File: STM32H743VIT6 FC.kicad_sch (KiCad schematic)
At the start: 82 parts, among them SW2 SW_Push, U1 TPS54302DDCR, U2 USBLC6-2SC6, U3 TPS54302DDCR

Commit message: W25N01GVZEIT
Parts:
- 3V3_C2: renamed from 3V3_C4; value 4u7 -> 1u
- U_FLASH1: value W25N01GVZEIG_TR -> W25N01GVZEIT
- renumbered 3v3_C3 to 3v3_C1
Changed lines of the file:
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@@
 		(on_board yes)
 		(dnp no)
-		(property "Reference" "3v3_C3"
+		(property "Reference" "3v3_C1"
 			(at 546.862 90.932 0)
 			(effects
@@
 			(project "STM32H743VIT6 FC"
 				(path "/c74cb3f0-4ada-468c-ba5c-2dfd9a4e418b"
-					(reference "3v3_C3")
+					(reference "3v3_C1")
 					(unit 1)
 				)
@@
 		(on_board yes)
 		(dnp no)
-		(property "Reference" "3V3_C4"
+		(property "Reference" "3V3_C2"
 			(at 586.74 90.17 0)
 			(effects
@@
 			)
 		)
-		(property "Value" "4u7"
+		(property "Value" "1u"
 			(at 586.74 92.71 0)
 			(effects
@@
 			(project "STM32H743VIT6 FC"
 				(path "/c74cb3f0-4ada-468c-ba5c-2dfd9a4e418b"
-					(reference "3V3_C4")
+					(reference "3V3_C2")
 					(unit 1)
 				)
@@
 			)
 		)
-		(property "Value" "W25N01GVZEIG_TR"
+		(property "Value" "W25N01GVZEIT"
 			(at 211.836 223.012 0)
 			(effects

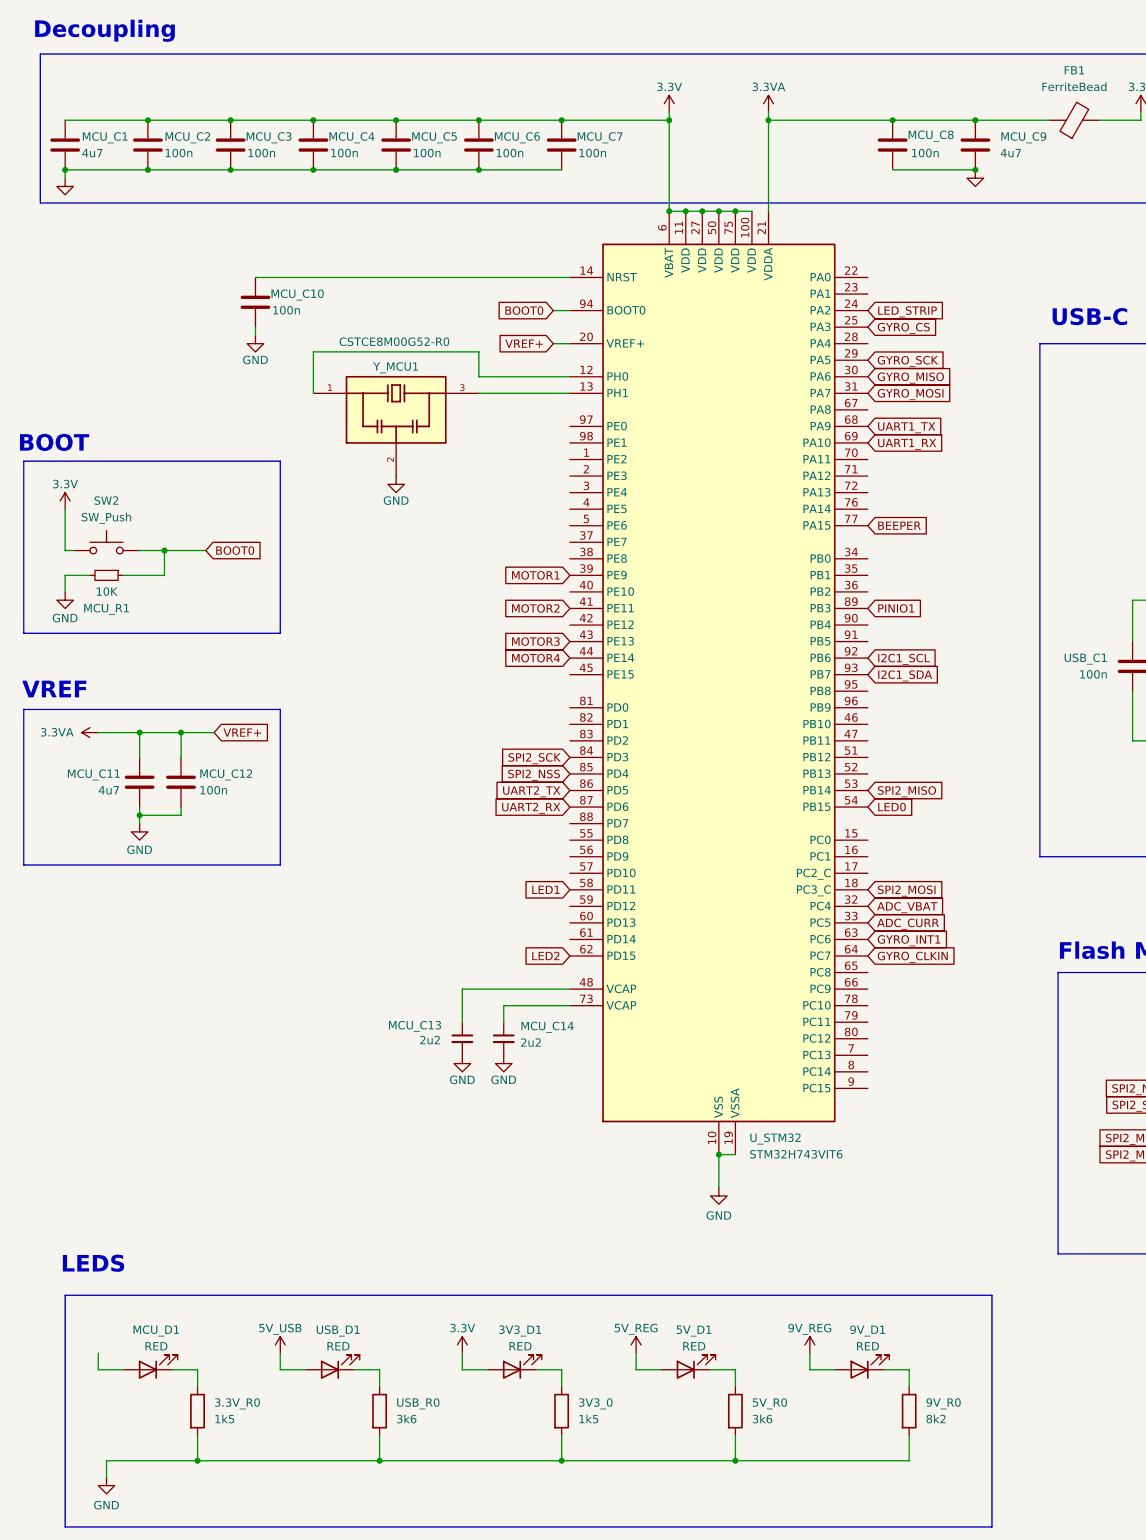
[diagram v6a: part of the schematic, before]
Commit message: Connected USB and fixed MCU decoupling.
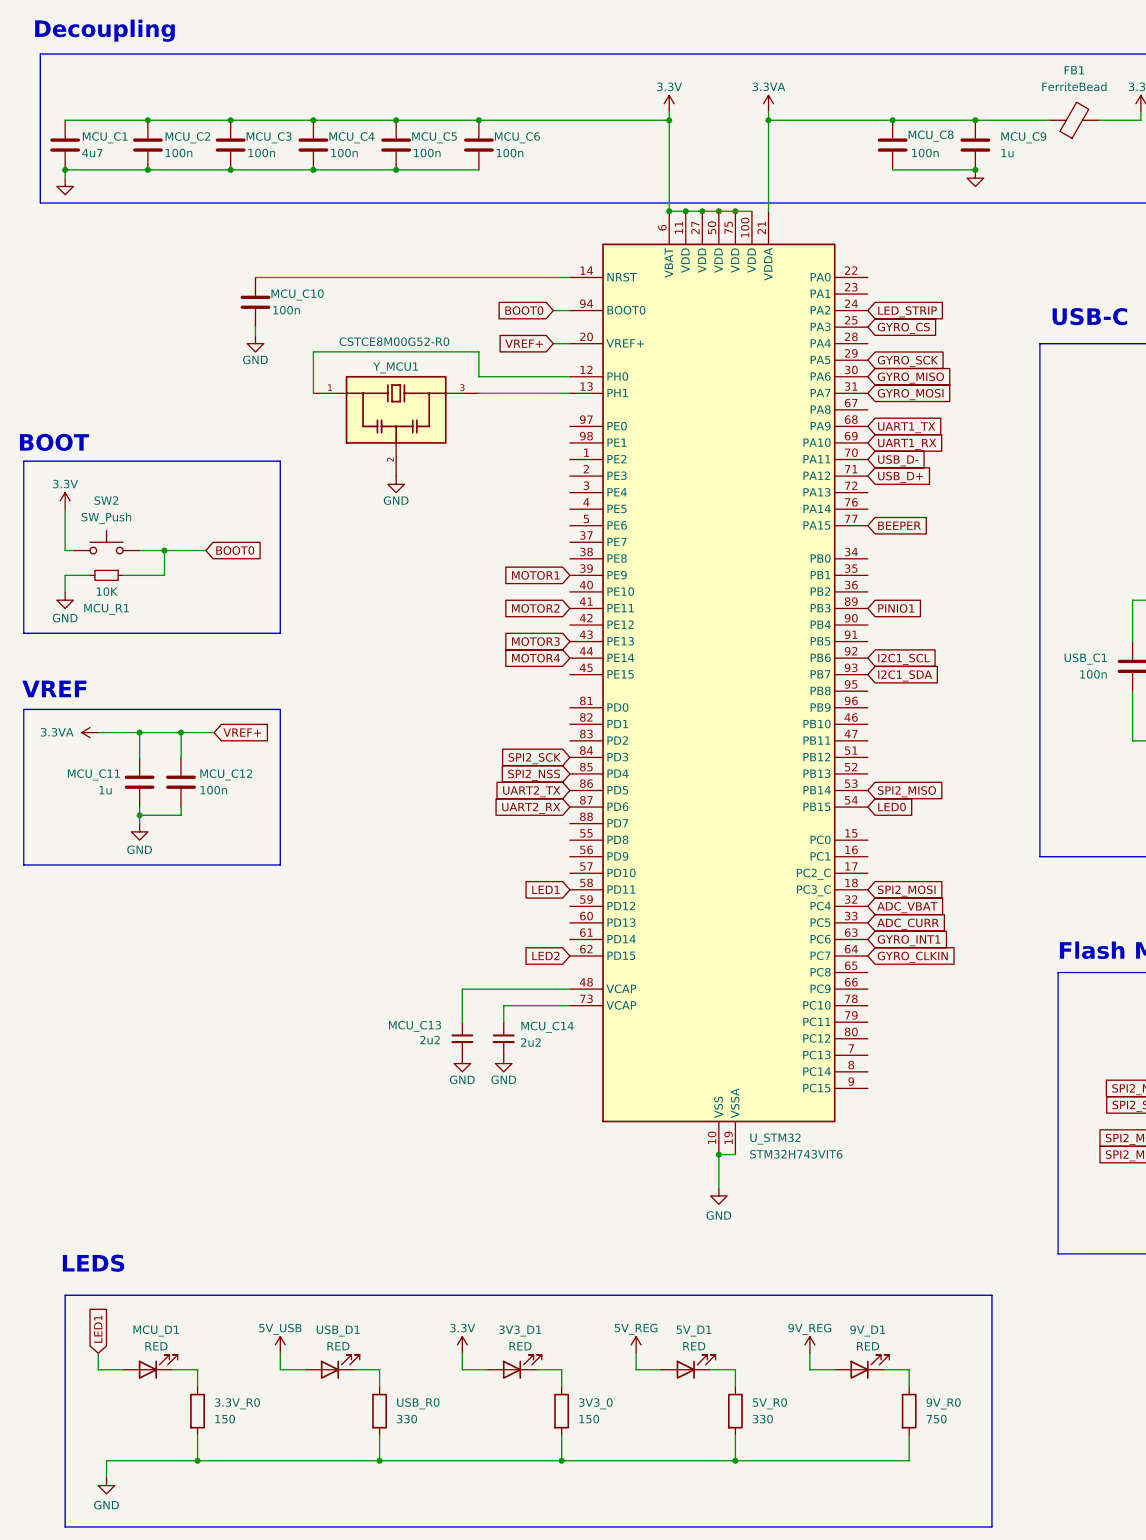
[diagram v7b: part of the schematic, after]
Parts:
- removed MCU_C7: 100n, Capacitor_SMD:C_0402_1005Metric, symbol Device:C
- 3.3V_R0, 3V3_0: value 1k5 -> 150
- 5V_R0, USB_R0: value 3k6 -> 330
- 9V_R0: value 8k2 -> 750
- MCU_C11, MCU_C9: value 4u7 -> 1u
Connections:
- net LED1: now also MCU_D1.2 (A)
- net USB_D+: now also U_STM32.71 (PA12)
- net USB_D-: now also U_STM32.70 (PA11)
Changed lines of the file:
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@@
 	)
 	(junction
-		(at 101.6 54.61)
-		(diameter 0)
-		(color 0 0 0 0)
-	)
-	(junction
 		(at 36.83 161.29)
 		(diameter 0)
@@
 	)
 	(junction
-		(at 88.9 62.23)
-		(diameter 0)
-		(color 0 0 0 0)
-	)
-	(junction
 		(at 363.22 213.614)
 		(diameter 0)
@@
 	(wire
 		(pts
-			(xy 101.6 54.61) (xy 118.11 54.61)
+			(xy 88.9 54.61) (xy 118.11 54.61)
 		)
 		(stroke
@@
 	(wire
 		(pts
-			(xy 88.9 54.61) (xy 101.6 54.61)
-		)
-		(stroke
-			(width 0)
-			(type default)
-		)
-	)
-	(wire
-		(pts
 			(xy 69.85 246.38) (xy 73.66 246.38)
 		)
@@
 	(wire
 		(pts
-			(xy 88.9 62.23) (xy 101.6 62.23)
-		)
-		(stroke
-			(width 0)
-			(type default)
-		)
-	)
-	(wire
-		(pts
 			(xy 728.98 71.12) (xy 740.41 71.12)
 		)
@@
 		)
 	)
+	(global_label "USB_D-"
+		(shape input)
+		(at 148.59 106.68 0)
+		(fields_autoplaced yes)
+		(effects
+			(font
+				(size 1.27 1.27)
+			)
+			(justify left)
+		)
+		(property "Intersheetrefs" "${INTERSHEET_REFS}"
+			(at 159.1952 106.68 0)
+			(effects
+				(font
+					(size 1.27 1.27)
+				)
+				(justify left)
+				(hide yes)
+			)
+		)
+	)
 	(global_label "GYRO_MOSI"
 		(shape input)
@@
 		)
 	)
+	(global_label "LED1"
+		(shape input)
+		(at 30.48 243.84 90)
+		(fields_autoplaced yes)
+		(effects
+			(font
+				(size 1.27 1.27)
+			)
+			(justify left)
+		)
+		(property "Intersheetrefs" "${INTERSHEET_REFS}"
+			(at 30.48 236.1982 90)
+			(effects
+				(font
+					(size 1.27 1.27)
+				)
+				(justify left)
+				(hide yes)
+			)
+		)
+	)
 	(global_label "GYRO_MOSI"
 		(shape input)
@@
 		)
 	)
+	(global_label "USB_D+"
+		(shape input)
+		(at 148.59 109.22 0)
+		(fields_autoplaced yes)
+		(effects
+			(font
+				(size 1.27 1.27)
+			)
+			(justify left)
+		)
+		(property "Intersheetrefs" "${INTERSHEET_REFS}"
+			(at 159.1952 109.22 0)
+			(effects
+				(font
+					(size 1.27 1.27)
+				)
+				(justify left)
+				(hide yes)
+			)
+		)
+	)
 	(global_label "SPI2_MOSI"
 		(shape input)
@@
 			)
 		)
-		(property "Value" "3k6"
+		(property "Value" "330"
 			(at 130.81 253.9999 0)
 			(effects
@@
 			)
 		)
-		(property "Value" "4u7"
+		(property "Value" "1u"
 			(at 30.48 157.48 0)
 			(effects
@@
 	(symbol
 		(lib_id "Device:C")
-		(at 101.6 58.42 0)
-		(unit 1)
-		(exclude_from_sim no)
-		(in_bom yes)
-		(on_board yes)
-		(dnp no)
-		(property "Reference" "MCU_C7"
-			(at 103.886 57.15 0)
-			(effects
-				(font
-					(size 1.27 1.27)
-				)
-				(justify left)
-			)
-		)
-		(property "Value" "100n"
-			(at 104.14 59.69 0)
-			(effects
-				(font
-					(size 1.27 1.27)
-				)
-				(justify left)
-			)
-		)
-		(property "Footprint" "Capacitor_SMD:C_0402_1005Metric"
-			(at 102.5652 62.23 0)
-			(effects
-				(font
-					(size 1.27 1.27)
-				)
-				(hide yes)
-			)
-		)
-		(property "Datasheet" "~"
-			(at 101.6 58.42 0)
-			(effects
-				(font
-					(size 1.27 1.27)
-				)
-				(hide yes)
-			)
-		)
-		(property "Description" "Unpolarized capacitor"
-			(at 101.6 58.42 0)
-			(effects
-				(font
-					(size 1.27 1.27)
-				)
-				(hide yes)
-			)
-		)
-		(property "LCSC Part" ""
-			(at 101.6 58.42 0)
-			(effects
-				(font
-					(size 1.27 1.27)
-				)
-				(hide yes)
-			)
-		)
-		(pin "2"
-		)
-		(pin "1"
-		)
-		(instances
-			(project "STM32H743VIT6 FC"
-				(path "/c74cb3f0-4ada-468c-ba5c-2dfd9a4e418b"
-					(reference "MCU_C7")
-					(unit 1)
-				)
-			)
-		)
-	)
-	(symbol
-		(lib_id "Device:C")
 		(at 43.18 156.21 0)
 		(unit 1)
@@
 			)
 		)
-		(property "Value" "1k5"
+		(property "Value" "150"
 			(at 48.26 253.9999 0)
 			(effects
@@
 			)
 		)
-		(property "Value" "8k2"
+		(property "Value" "750"
 			(at 157.48 253.9999 0)
 			(effects
@@
 			)
 		)
-		(property "Value" "1k5"
+		(property "Value" "150"
 			(at 104.14 253.9999 0)
 			(effects
@@
 			)
 		)
-		(property "Value" "3k6"
+		(property "Value" "330"
 			(at 76.2 253.9999 0)
 			(effects
@@
 			)
 		)
-		(property "Value" "4u7"
+		(property "Value" "1u"
 			(at 168.91 59.6899 0)
 			(effects

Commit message: conns
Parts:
- added AVTX_J1, GPS_J1, VTX_J1: Conn_01x06_Pin, symbol Connector:Conn_01x06_Pin
- added CAM_J1, LED_J1: Conn_01x03_Pin, symbol Connector:Conn_01x03_Pin
- added DEBUG_J1, RX_J1, UART2_J1: Conn_01x04_Pin, symbol Connector:Conn_01x04_Pin
- added ESC_J1: Conn_01x08_Pin, symbol Connector:Conn_01x08_Pin
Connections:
- net 3.3V: now also DEBUG_J1.4 (Pin_4)
- net 5V: now also GPS_J1.3 (Pin_3), RX_J1.3 (Pin_3)
- net 5V_REG: now also AVTX_J1.5 (Pin_5), CAM_J1.3 (Pin_3), LED_J1.1 (Pin_1), UART2_J1.3 (Pin_3)
- net 9V_REG: now also AVTX_J1.1 (Pin_1), VTX_J1.1 (Pin_1)
- net ADC_CURR: now also ESC_J1.7 (Pin_7)
- net BAT: now also ESC_J1.2 (Pin_2)
- net GND: now also AVTX_J1.6 (Pin_6), CAM_J1.2 (Pin_2), DEBUG_J1.3 (Pin_3), ESC_J1.1 (Pin_1), GPS_J1.4 (Pin_4), LED_J1.3 (Pin_3), RX_J1.4 (Pin_4), UART2_J1.4 (Pin_4), VTX_J1.2 (Pin_2), VTX_J1.5 (Pin_5)
- net I2C1_SCL: now also GPS_J1.2 (Pin_2)
- net I2C1_SDA: now also GPS_J1.1 (Pin_1)
- net LED_STRIP: now also LED_J1.2 (Pin_2)
- net MOTOR1: now also ESC_J1.3 (Pin_3)
- net MOTOR2: now also ESC_J1.4 (Pin_4)
- net MOTOR3: now also ESC_J1.5 (Pin_5)
- net MOTOR4: now also ESC_J1.6 (Pin_6)
- net UART1_RX: now also RX_J1.2 (Pin_2)
- net UART1_TX: now also RX_J1.1 (Pin_1)
- net UART2_RX: now also UART2_J1.2 (Pin_2)
- net UART2_TX: now also UART2_J1.1 (Pin_1)
- new net CAM: AVTX_J1.2 (Pin_2), CAM_J1.1 (Pin_1)
- new net SWCLK: DEBUG_J1.1 (Pin_1)
- new net SWDIO: DEBUG_J1.2 (Pin_2)
- new net UART3_RX: VTX_J1.4 (Pin_4)
- new net UART3_TX: VTX_J1.3 (Pin_3)
- new net UART4_RX: AVTX_J1.4 (Pin_4)
- new net UART4_TX: AVTX_J1.3 (Pin_3)
- new net UART5_RX: VTX_J1.6 (Pin_6)
- new net UART7_RX: ESC_J1.8 (Pin_8)
- new net UART8_RX: GPS_J1.6 (Pin_6)
- new net UART8_TX: GPS_J1.5 (Pin_5)
- no-connect marks 8 -> 58
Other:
- note added: "Connectors"
- moved on the sheet: 3.3V_R0, 3V3_0, 3V3_C2, 3V3_D1, 3v3_C1, 5V_C10, 5V_C11, 5V_C12, 5V_C7, 5V_C8, 5V_C9, 5V_D1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
